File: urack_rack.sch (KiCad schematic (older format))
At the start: 9 parts

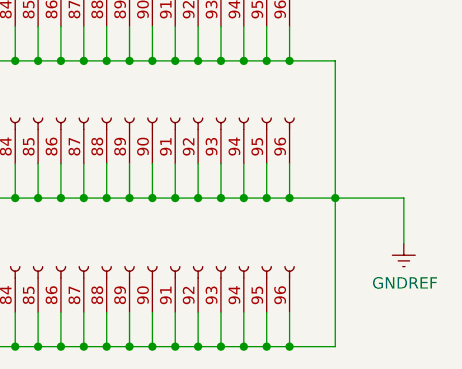
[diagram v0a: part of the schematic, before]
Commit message: Исправленны абсолютные пути на отнасительные
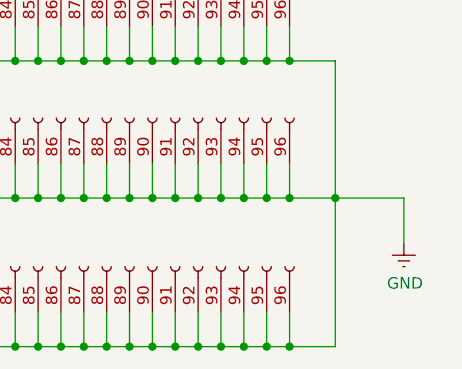
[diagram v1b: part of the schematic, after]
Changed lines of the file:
@@
 EESchema Schematic File Version 4
-LIBS:urack_rack-cache
 EELAYER 26 0
 EELAYER END
@@
 	10450 5400 10450 6050
 $Comp
-L uRack:GNDREF #PWR0101
+L uRack:GND #PWR0101
 U 1 1 5CACD69A
 P 10750 5600
 F 0 "#PWR0101" H 10750 5350 50  0001 C CNN
-F 1 "GNDREF" H 10755 5427 50  0000 C CNN
+F 1 "GND" H 10755 5427 50  0000 C CNN
 F 2 "" H 10750 5600 50  0001 C CNN
 F 3 "" H 10750 5600 50  0001 C CNN
